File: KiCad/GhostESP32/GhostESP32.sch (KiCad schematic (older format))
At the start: 40 parts, among them P1 USB_OTG, P2 CONN_02X30, Q1 Q_NPN_BCE, Q2 Q_NPN_BCE, SW1 SW_Push, SW2 SW_Push, U1 MC33269, U2 LM358, U3 CP2102, U4 ESP-WROOM-32

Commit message: Started routing the GhostESP32 board
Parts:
- C1, C10, C11, C2, C3, C4, C5, C6, C7, C8, C9: footprint (none) -> Capacitors_SMD:C_0603
- D1, D3, D4: footprint (none) -> LEDs:LED_0603
- D2: footprint (none) -> Diodes_SMD:D_SMA_Standard
- P1: footprint (none) -> Connectors:USB_Micro-B
- P2: footprint (none) -> hrs-fx8c:hrs-fx8c-60p-sv
- Q1, Q2: footprint (none) -> TO_SOT_Packages_SMD:SOT-23
- R1, R10, R11, R12, R13, R14, R15, R2, R3, R4, R5, R6, R7, R8, R9: footprint (none) -> Resistors_SMD:R_0603
- SW1, SW2: footprint (none) -> Buttons_Switches_SMD:SW_SPST_EVQP2
- U1: footprint (none) -> TO_SOT_Packages_SMD:TO-252-2Lead
- U2: footprint (none) -> Housings_SOIC:SOIC-8_3.9x4.9mm_Pitch1.27mm
- U3: footprint (none) -> Housings_DFN_QFN:QFN-28-1EP_5x5mm_Pitch0.5mm
- U4: footprint (none) -> NorBotKiCadFootprints:ESP32-WROOM
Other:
- note added: "MMBT2222A NPN transistors\nFarnell no: 177-3626"
- moved on the sheet: D2, D3, D4, P1, R10, R8, U2A, U2B

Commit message: Spent hours doing routing...
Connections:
- net +3V3: now also P2.2 (P2), P2.4 (P4); no longer P2.1 (P1)
- net +5V: now also P2.20 (P20), P2.21 (P21), P2.22 (P22), P2.23 (P23), P2.24 (P24), P2.7 (P7), P2.9 (P9); no longer P2.10 (P10), P2.2 (P2), P2.4 (P4), P2.6 (P6)
- net CLK: now also P2.46 (P46); no longer P2.51 (P51)
- net CMD: now also P2.47 (P47); no longer P2.49 (P49)
- net GND: now also P2.11 (P11), P2.13 (P13), P2.15 (P15), P2.26 (P26), P2.27 (P27), P2.28 (P28), P2.29 (P29), P2.30 (P30), P2.41 (P41); no longer P2.35 (P35), P2.36 (P36), P2.37 (P37), P2.38 (P38), P2.39 (P39), P2.40 (P40), P2.7 (P7), P2.9 (P9)
- net IO0: now also P2.40 (P40); no longer P2.23 (P23)
- net IO12: now also P2.51 (P51); no longer P2.18 (P18)
- net IO14: now also P2.52 (P52); no longer P2.20 (P20)
- net IO15: now also P2.43 (P43); no longer P2.53 (P53)
- net IO16: now also P2.38 (P38); no longer P2.17 (P17)
- net IO17: now also P2.37 (P37); no longer P2.15 (P15)
- net IO18: now also P2.35 (P35); no longer P2.25 (P25)
- net IO19: now also P2.34 (P34); no longer P2.27 (P27)
- net IO2: now also P2.42 (P42); no longer P2.55 (P55)
- net IO21: now also P2.33 (P33); no longer P2.29 (P29)
- net IO22: now also P2.32 (P32); no longer P2.13 (P13)
- net IO23: now also P2.31 (P31); no longer P2.11 (P11)
- net IO25: now also P2.55 (P55); no longer P2.26 (P26)
- net IO26: now also P2.54 (P54); no longer P2.24 (P24)
- net IO27: now also P2.53 (P53); no longer P2.22 (P22)
- net IO32: now also P2.57 (P57); no longer P2.30 (P30)
- net IO33: now also P2.56 (P56); no longer P2.28 (P28)
- net IO34: now also P2.59 (P59); no longer P2.34 (P34)
- net IO35: now also P2.58 (P58); no longer P2.32 (P32)
- net IO4: now also P2.39 (P39); no longer P2.21 (P21)
- net IO5: now also P2.36 (P36); no longer P2.19 (P19)
- net SD0: now also P2.45 (P45); no longer P2.43 (P43)
- net SD1: now also P2.44 (P44); no longer P2.41 (P41)
- net SD2: now also P2.49 (P49); no longer P2.45 (P45)
- net SD3: now also P2.48 (P48); no longer P2.47 (P47)
- net SENSOR_VN: now also P2.60 (P60); no longer P2.31 (P31)
- net SENSOR_VP: now also P2.1 (P1); no longer P2.33 (P33)
- net USB_SUSPEND: now also P2.18 (P18); no longer P2.42 (P42)
- no-connect marks 17 -> 13

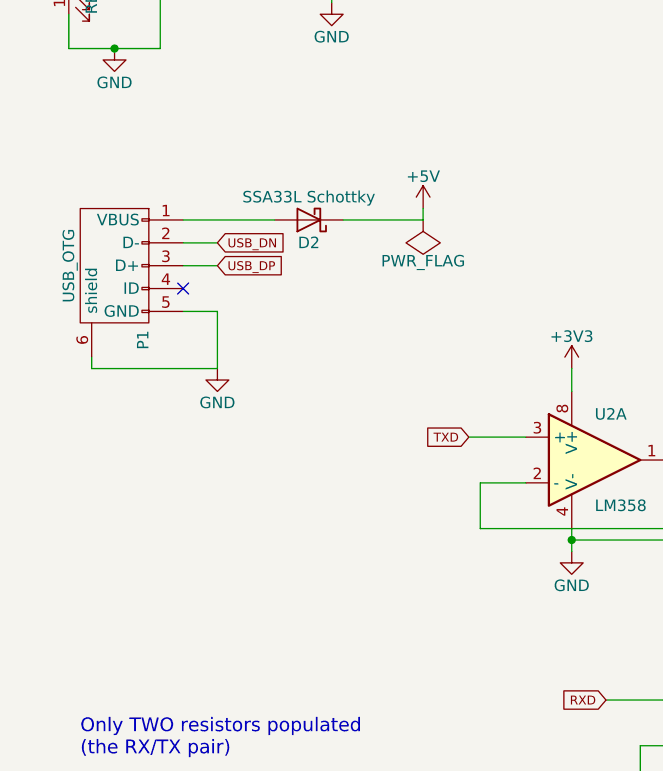
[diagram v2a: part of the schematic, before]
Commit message: GhostESP32 and GhostSensorboard mostly done - but with wrong 60 pin connector
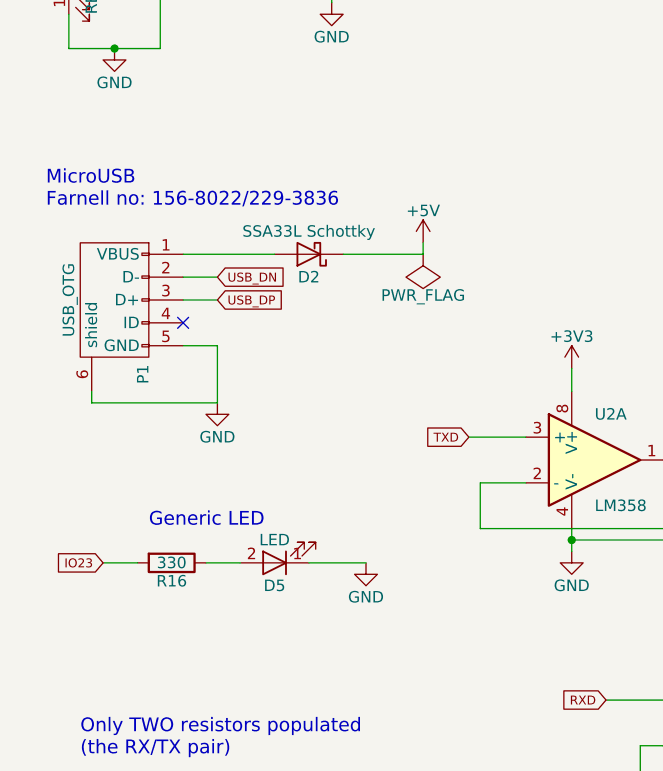
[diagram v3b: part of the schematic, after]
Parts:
- added D5: LED, LEDs:LED_0603, symbol LED
- added R16: 330, Resistors_SMD:R_0603, symbol R
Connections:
- net GND: now also D5.1 (K)
- net IO23: now also R16.2
- new net: D5.2 (A), R16.1
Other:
- note added: "Generic LED"
- note added: "MicroUSB\nFarnell no: 156-8022/229-3836"
- moved on the sheet: D2, P1
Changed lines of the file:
@@
 L USB_OTG P1
 U 1 1 5893902B
-P 950 2850
-F 0 "P1" H 1275 2725 50  0000 C CNN
-F 1 "USB_OTG" H 950 3050 50  0000 C CNN
-F 2 "Connectors:USB_Micro-B" V 900 2750 50  0001 C CNN
-F 3 "" V 900 2750 50  0000 C CNN
-	1    950  2850
+P 950 3000
+F 0 "P1" H 1275 2875 50  0000 C CNN
+F 1 "USB_OTG" H 950 3200 50  0000 C CNN
+F 2 "Connectors:USB_Micro-B" V 900 2900 50  0001 C CNN
+F 3 "" V 900 2900 50  0000 C CNN
+	1    950  3000
 	0    -1   1    0
 $EndComp
@@
 L GND #PWR027
 U 1 1 5895DDF4
-P 1400 3300
-F 0 "#PWR027" H 1400 3050 50  0001 C CNN
-F 1 "GND" H 1400 3150 50  0000 C CNN
-F 2 "" H 1400 3300 50  0000 C CNN
-F 3 "" H 1400 3300 50  0000 C CNN
-	1    1400 3300
-	1    0    0    -1
-$EndComp
-Wire Wire Line
-	1400 3300 850  3300
-Wire Wire Line
-	850  3300 850  3250
-Wire Wire Line
-	1250 3050 1400 3050
-Wire Wire Line
-	1400 3050 1400 3300
+P 1400 3450
+F 0 "#PWR027" H 1400 3200 50  0001 C CNN
+F 1 "GND" H 1400 3300 50  0000 C CNN
+F 2 "" H 1400 3450 50  0000 C CNN
+F 3 "" H 1400 3450 50  0000 C CNN
+	1    1400 3450
+	1    0    0    -1
+$EndComp
+Wire Wire Line
+	1400 3450 850  3450
+Wire Wire Line
+	850  3450 850  3400
+Wire Wire Line
+	1250 3200 1400 3200
+Wire Wire Line
+	1400 3200 1400 3450
 $Comp
 L D_Schottky D2
 U 1 1 5895E8E3
-P 1800 2650
-F 0 "D2" H 1800 2750 50  0000 C CNN
-F 1 "SSA33L Schottky" H 1800 2550 50  0000 C CNN
-F 2 "Diodes_SMD:D_SMA_Standard" H 1800 2650 50  0001 C CNN
-F 3 "" H 1800 2650 50  0000 C CNN
-	1    1800 2650
+P 1800 2800
+F 0 "D2" H 1800 2900 50  0000 C CNN
+F 1 "SSA33L Schottky" H 1800 2700 50  0000 C CNN
+F 2 "Diodes_SMD:D_SMA_Standard" H 1800 2800 50  0001 C CNN
+F 3 "" H 1800 2800 50  0000 C CNN
+	1    1800 2800
 	-1   0    0    1
 $EndComp
 Wire Wire Line
-	1650 2650 1250 2650
-Wire Wire Line
-	1950 2650 2300 2650
-Text GLabel 1400 2850 2    39   Input ~ 0
+	1650 2800 1250 2800
+Wire Wire Line
+	1950 2800 2300 2800
+Text GLabel 1400 3000 2    39   Input ~ 0
 USB_DP
-Text GLabel 1400 2750 2    39   Input ~ 0
+Text GLabel 1400 2900 2    39   Input ~ 0
 USB_DN
-NoConn ~ 1250 2950
-Wire Wire Line
-	1400 2850 1250 2850
-Wire Wire Line
-	1250 2750 1400 2750
+NoConn ~ 1250 3100
+Wire Wire Line
+	1400 3000 1250 3000
+Wire Wire Line
+	1250 2900 1400 2900
 $Comp
 L LED D1
@@
 L +5V #PWR040
 U 1 1 5898C3A8
-P 2300 2600
-F 0 "#PWR040" H 2300 2450 50  0001 C CNN
-F 1 "+5V" H 2300 2740 50  0000 C CNN
-F 2 "" H 2300 2600 50  0000 C CNN
-F 3 "" H 2300 2600 50  0000 C CNN
-	1    2300 2600
-	1    0    0    -1
-$EndComp
-Wire Wire Line
-	2300 2650 2300 2600
+P 2300 2750
+F 0 "#PWR040" H 2300 2600 50  0001 C CNN
+F 1 "+5V" H 2300 2890 50  0000 C CNN
+F 2 "" H 2300 2750 50  0000 C CNN
+F 3 "" H 2300 2750 50  0000 C CNN
+	1    2300 2750
+	1    0    0    -1
+$EndComp
+Wire Wire Line
+	2300 2800 2300 2750
 $Comp
 L +5V #PWR041
@@
 L PWR_FLAG #FLG043
 U 1 1 5899E941
-P 2300 2650
-F 0 "#FLG043" H 2300 2745 50  0001 C CNN
-F 1 "PWR_FLAG" H 2300 2830 50  0000 C CNN
-F 2 "" H 2300 2650 50  0000 C CNN
-F 3 "" H 2300 2650 50  0000 C CNN
-	1    2300 2650
+P 2300 2800
+F 0 "#FLG043" H 2300 2895 50  0001 C CNN
+F 1 "PWR_FLAG" H 2300 2980 50  0000 C CNN
+F 2 "" H 2300 2800 50  0000 C CNN
+F 3 "" H 2300 2800 50  0000 C CNN
+	1    2300 2800
 	-1   0    0    1
 $EndComp
@@
 	9900 5700 9800 5700
 NoConn ~ 10550 5600
+$Comp
+L LED D5
+U 1 1 589FED00
+P 1650 4150
+F 0 "D5" H 1650 4250 50  0000 C CNN
+F 1 "LED" H 1650 4050 50  0000 C CNN
+F 2 "LEDs:LED_0603" H 1650 4150 50  0001 C CNN
+F 3 "" H 1650 4150 50  0000 C CNN
+	1    1650 4150
+	-1   0    0    1
+$EndComp
+$Comp
+L R R16
+U 1 1 589FF420
+P 1200 4150
+F 0 "R16" V 1280 4150 50  0000 C CNN
+F 1 "330" V 1200 4150 50  0000 C CNN
+F 2 "Resistors_SMD:R_0603" V 1130 4150 50  0001 C CNN
+F 3 "" H 1200 4150 50  0000 C CNN
+	1    1200 4150
+	0    1    1    0
+$EndComp
+$Comp
+L GND #PWR054
+U 1 1 58A0017B
+P 2050 4150
+F 0 "#PWR054" H 2050 3900 50  0001 C CNN
+F 1 "GND" H 2050 4000 50  0000 C CNN
+F 2 "" H 2050 4150 50  0000 C CNN
+F 3 "" H 2050 4150 50  0000 C CNN
+	1    2050 4150
+	1    0    0    -1
+$EndComp
+Wire Wire Line
+	900  4150 1050 4150
+Wire Wire Line
+	1350 4150 1500 4150
+Wire Wire Line
+	1800 4150 2050 4150
+Text Notes 1100 4000 0    60   ~ 0
+Generic LED
+Text GLabel 900  4150 0    39   Input ~ 0
+IO23
+Text Notes 650  2600 0    60   ~ 0
+MicroUSB\nFarnell no: 156-8022/229-3836
 $EndSCHEMATC

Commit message: Routing finished. Playing around with BOM as XSL file.
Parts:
- P1: symbol USB_OTG -> USB_OTG-RESCUE-GhostESP32
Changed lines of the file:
@@
 EESchema Schematic File Version 2
+LIBS:GhostESP32-rescue
 LIBS:power
 LIBS:device
@@
 LIBS:switches
 LIBS:GhostESP32-cache
-EELAYER 25 0
+EELAYER 26 0
 EELAYER END
 $Descr A4 11693 8268
 encoding utf-8
 Sheet 1 1
-Title ""
-Date ""
-Rev ""
-Comp ""
+Title "Ghost ESP32"
+Date "2017-02-25"
+Rev "1"
+Comp "Frode Lillerud"
 Comment1 ""
 Comment2 ""
@@
 A shield based around the ESP-WROOM-32\nIt uses a stackable header from Hirose to connect to other boards.\nBoard is powered by 5.0V either through MicroUSB, or via 60-pin connector, or by separate power pins.
 $Comp
-L USB_OTG P1
+L USB_OTG-RESCUE-GhostESP32 P1
 U 1 1 5893902B
 P 950 3000

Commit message: Both boards done, and sent to Elecrow.
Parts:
- removed Q1, Q2: Q_NPN_BCE, TO_SOT_Packages_SMD:SOT-23, symbol Q_NPN_BCE
- added Q1, Q2: Q_NPN_BEC, symbol Q_NPN_BEC
- R16: value 330 -> 390
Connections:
- net DTR: now also Q2.2 (E)
- net EN: now also Q1.3 (C)
- net IO0: now also Q2.3 (C)
- net RTS: now also Q1.2 (E)
- net at R2.1: now also Q1.1 (B)
- net at R3.1: now also Q2.1 (B)
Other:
- note added: "A shield based around the ESP-WROOM-32\nIt uses a stackable header from Hirose to connect to other boards.\nBoard is powered by 5.0V either through MicroUSB, or via 60-pin connector."
- note added: "MC33269DT-3.3G\nFarnel no: 165-2330\n1.1V dropout, 800mA out"
- note added: "Topside connector, 60 pin\nHirose FX8C-60P-SV\nFarnell no: 249-8646"
- note removed: "A shield based around the ESP-WROOM-32\nIt uses a stackable header from Hirose to connect to other boards.\nBoard is powered by 5.0V either through MicroUSB, or via 60-pin connector, or by separate power pins."
- note removed: "TODO: Doublecheck pins!! And which NPN should I use?"
- note removed: "Topside connector, 40 pin\nHirose FX8C-40S-SV5\nFarnell no: 249-8688"
- moved on the sheet: P2

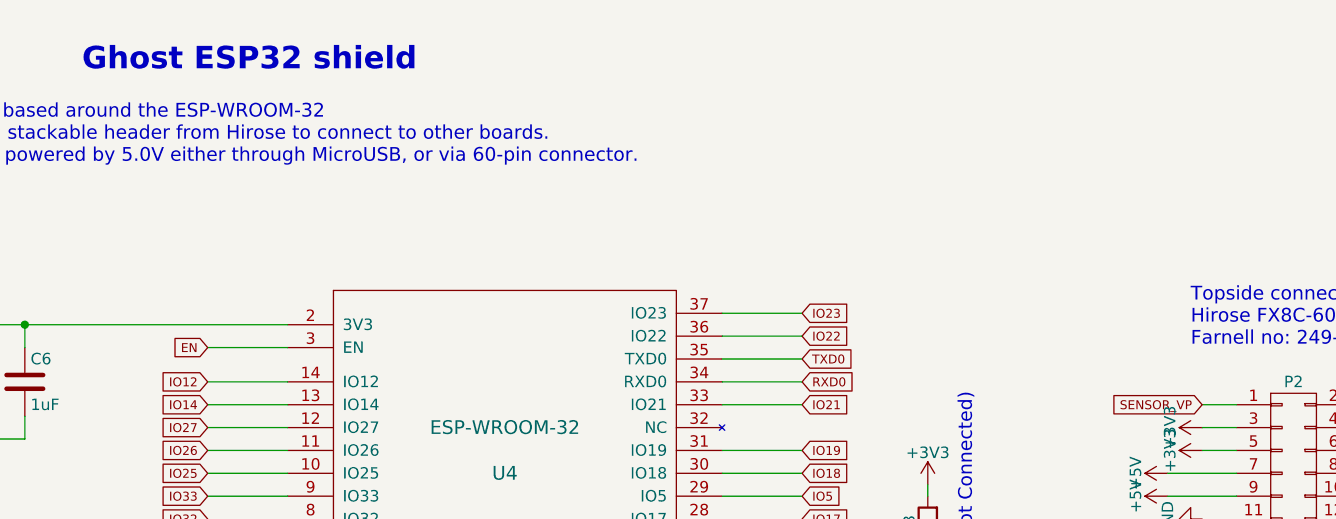
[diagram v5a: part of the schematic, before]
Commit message: Comments about pins 34-39 and 6-11.
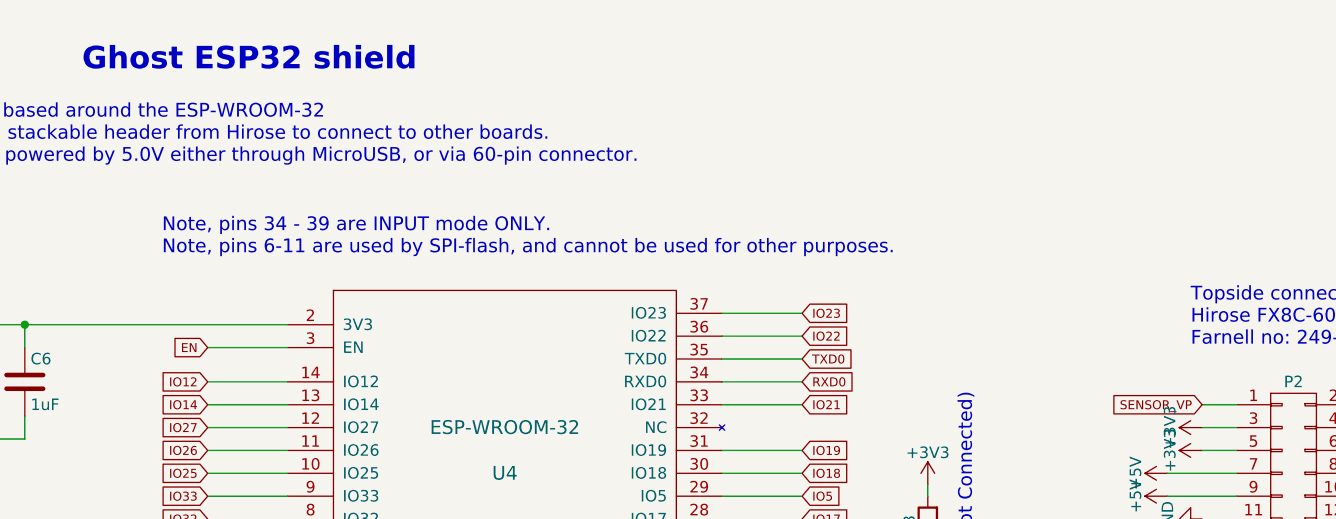
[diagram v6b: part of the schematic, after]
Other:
- note added: "Note, pins 34 - 39 are INPUT mode ONLY.\nNote, pins 6-11 are used by SPI-flash, and cannot be used for other purposes."
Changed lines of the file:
@@
 Text Notes 2050 1950 0    60   ~ 0
 MC33269DT-3.3G\nFarnel no: 165-2330\n1.1V dropout, 800mA out
+Text Notes 5200 1600 0    60   ~ 0
+Note, pins 34 - 39 are INPUT mode ONLY.\nNote, pins 6-11 are used by SPI-flash, and cannot be used for other purposes.
 $EndSCHEMATC
